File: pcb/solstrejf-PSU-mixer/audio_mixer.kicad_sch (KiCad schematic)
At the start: 9 parts, among them U1 Opamp_Dual

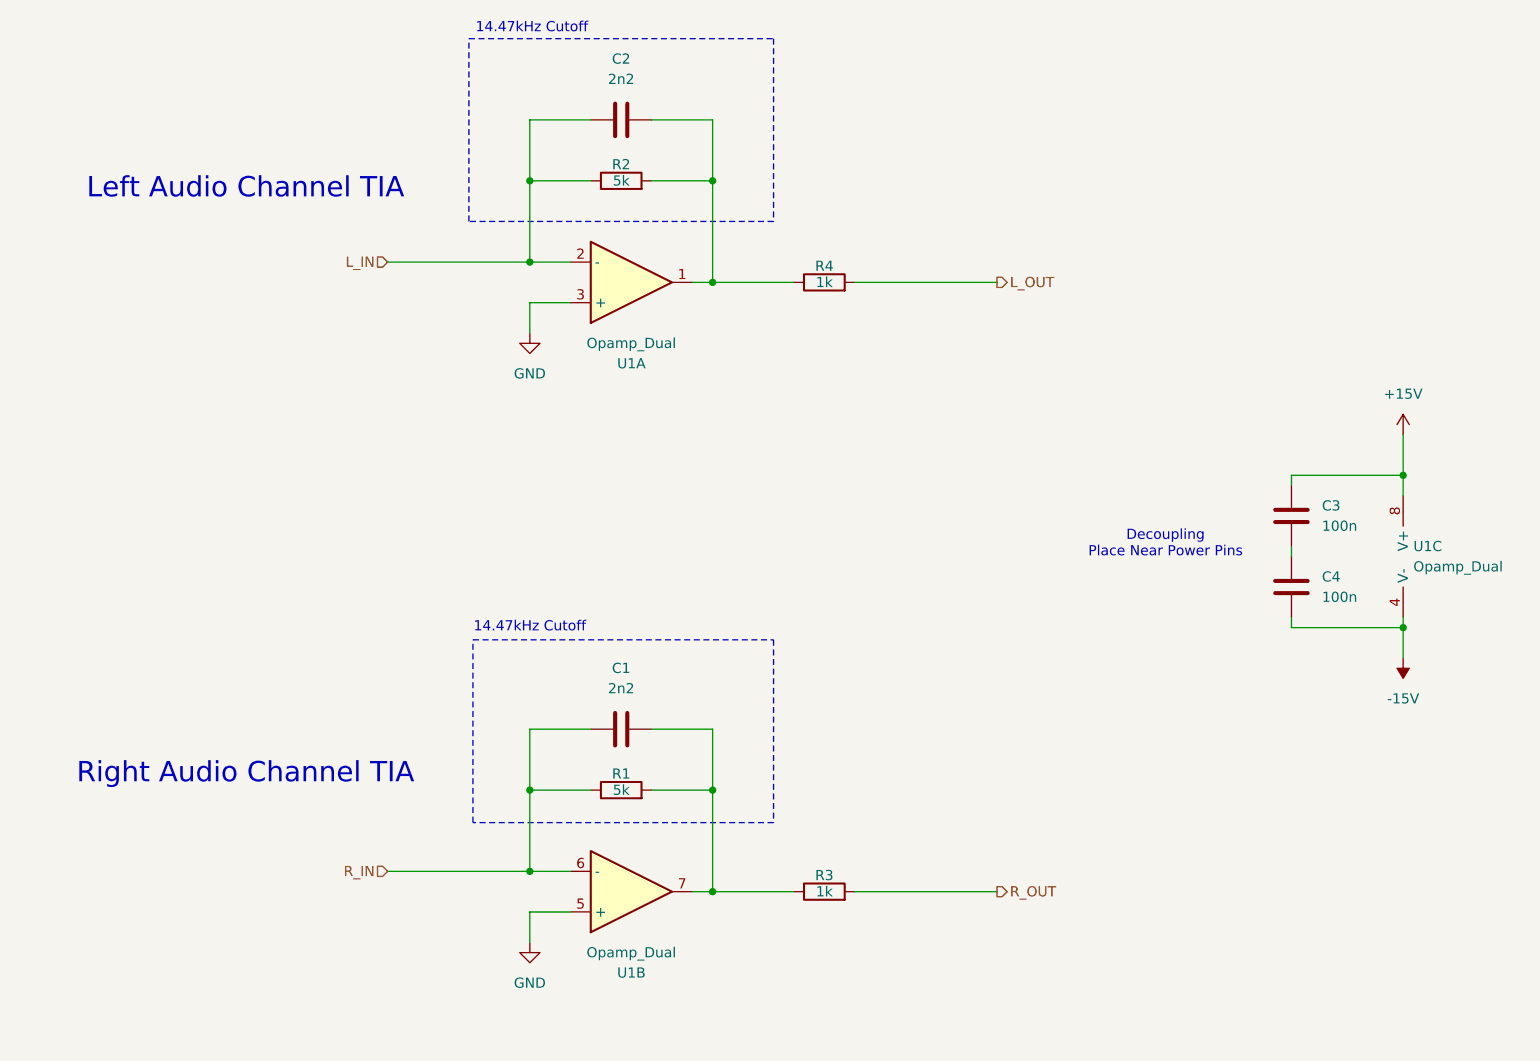
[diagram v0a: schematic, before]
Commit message: updated KiCad schematic and PCB with the new changes added to the TIA after LTspice simulations.
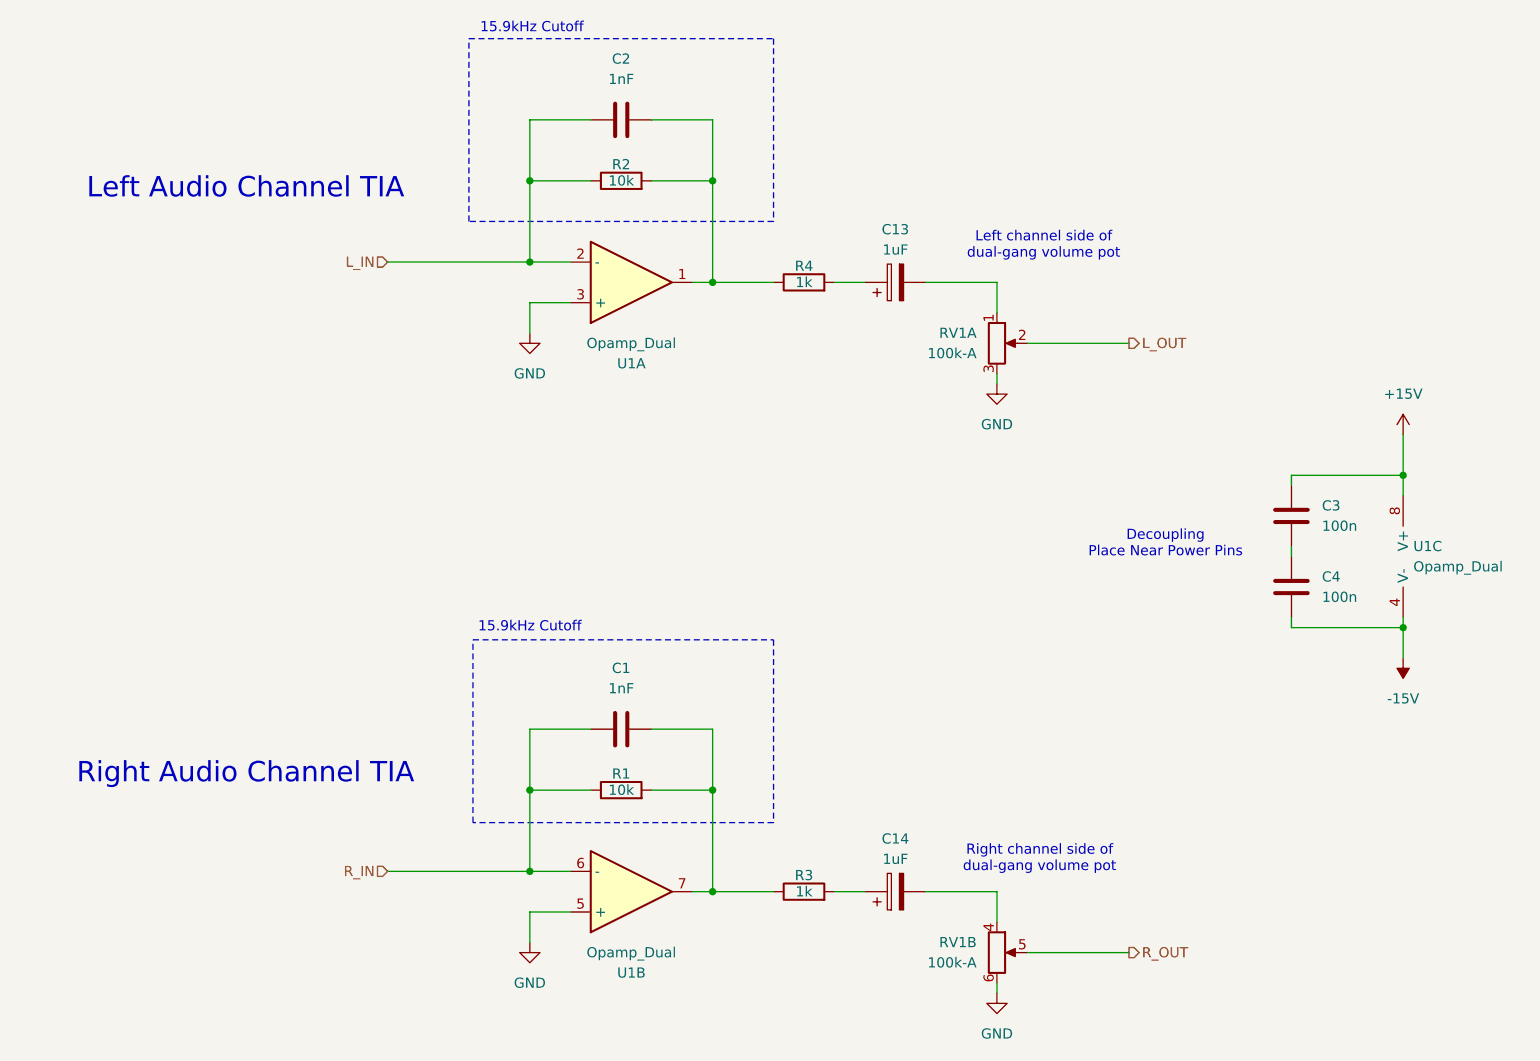
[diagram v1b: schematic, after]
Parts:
- added C13, C14: 1uF, Capacitor_THT:CP_Radial_D5.0mm_P2.00mm, symbol Device:C_Polarized
- added RV1: 100k-A, Connector_PinHeader_2.54mm:PinHeader_2x03_P2.54mm_Vertical, symbol Device:R_Potentiometer_Dual_Separate
- C1, C2: value 2n2 -> 1nF
- R1, R2: value 5k -> 10k
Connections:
- net GND: now also RV1.3, RV1.6
- net L_OUT: now also RV1.2; no longer R4.2
- net R_OUT: now also RV1.5; no longer R3.2
- new net: C14.1, R3.2
- new net: C13.2, RV1.1
- new net: C13.1, R4.2
- new net: C14.2, RV1.4
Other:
- note added: "15.9kHz Cutoff"
- note added: "Left channel side of dual-gang volume pot"
- note added: "Right channel side of dual-gang volume pot"
- note removed: "14.47kHz Cutoff"
- moved on the sheet: R3, R4

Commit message: made first attempt of a PCB layout onf the PSU/mixer. No routing performed. Minor updates to schematic, including mounting holes.
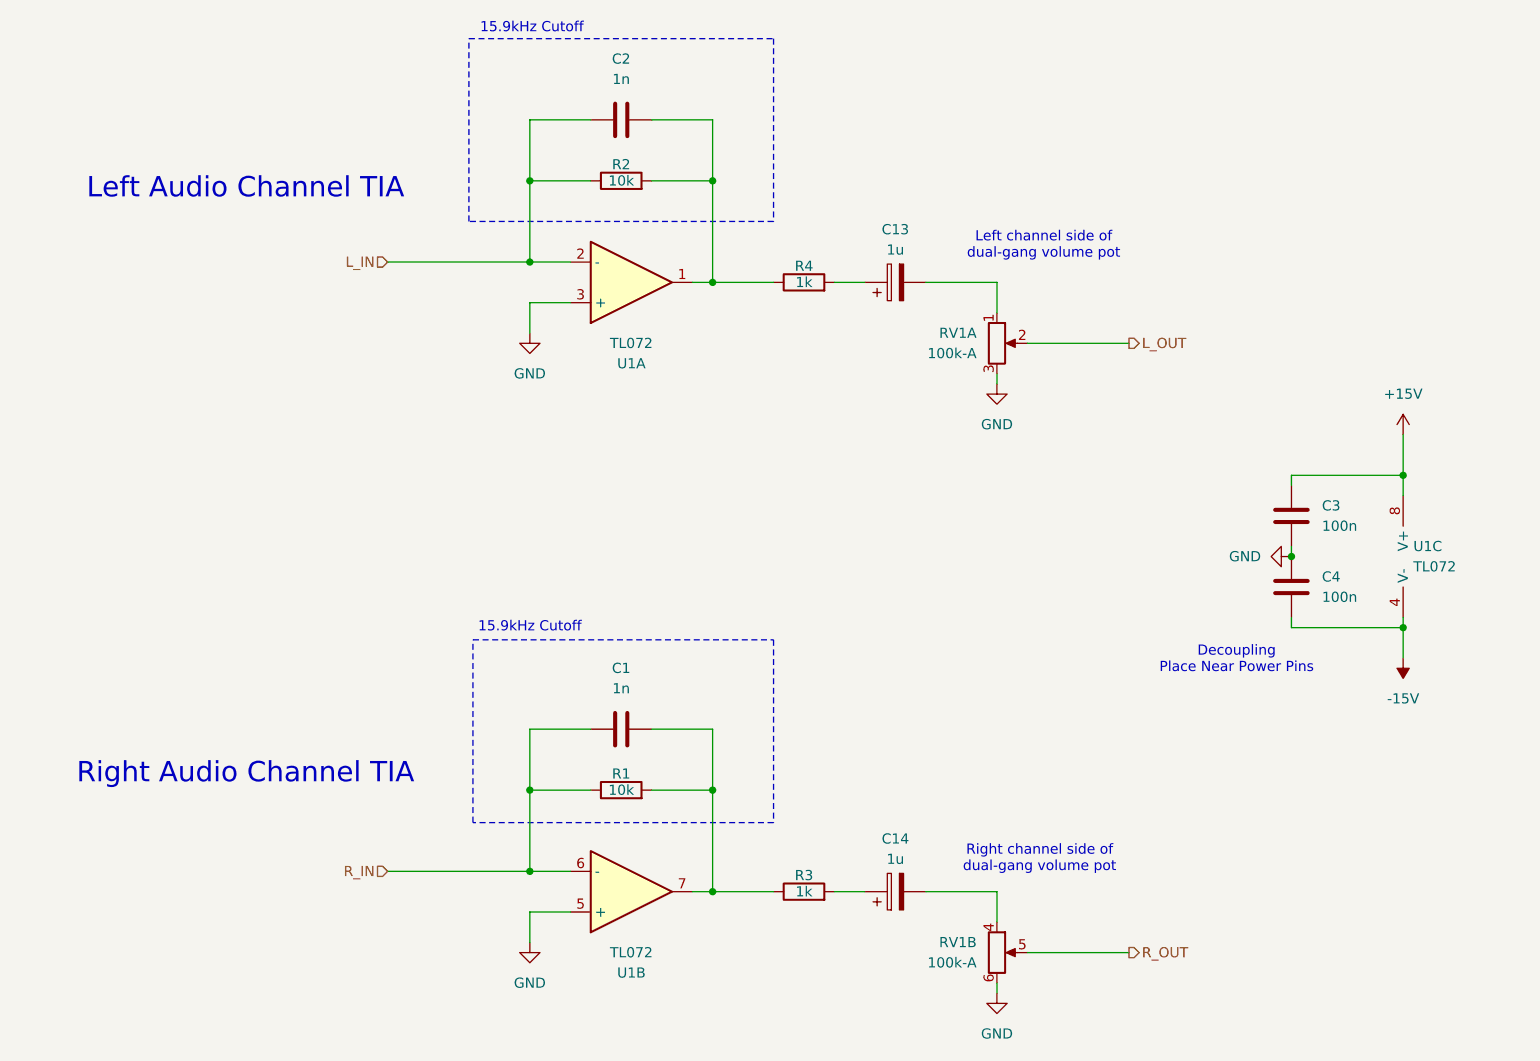
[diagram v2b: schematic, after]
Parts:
- C1, C2: value 1nF -> 1n
- C13, C14: value 1uF -> 1u
- U1: value Opamp_Dual -> TL072
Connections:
- net GND: now also C3.1, C4.2
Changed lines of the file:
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@@
+	)
+	(junction
+		(at 214.63 90.17)
+		(diameter 0)
+		(color 0 0 0 0)
 	)
 	(junction
@@
 	(text "Decoupling\nPlace Near Power Pins"
 		(exclude_from_sim no)
-		(at 198.882 88.646 0)
+		(at 207.772 103.124 0)
 		(effects
 			(font
@@
 	(symbol
 		(lib_id "power:GND")
+		(at 214.63 90.17 270)
+		(unit 1)
+		(exclude_from_sim no)
+		(in_bom yes)
+		(on_board yes)
+		(dnp no)
+		(fields_autoplaced yes)
+		(property "Reference" "#PWR026"
+			(at 208.28 90.17 0)
+			(effects
+				(font
+					(size 1.27 1.27)
+				)
+				(hide yes)
+			)
+		)
+		(property "Value" "GND"
+			(at 210.82 90.1699 90)
+			(effects
+				(font
+					(size 1.27 1.27)
+				)
+				(justify right)
+			)
+		)
+		(property "Footprint" ""
+			(at 214.63 90.17 0)
+			(effects
+				(font
+					(size 1.27 1.27)
+				)
+				(hide yes)
+			)
+		)
+		(property "Datasheet" ""
+			(at 214.63 90.17 0)
+			(effects
+				(font
+					(size 1.27 1.27)
+				)
+				(hide yes)
+			)
+		)
+		(property "Description" "Power symbol creates a global label with name \"GND\" , ground"
+			(at 214.63 90.17 0)
+			(effects
+				(font
+					(size 1.27 1.27)
+				)
+				(hide yes)
+			)
+		)
+		(pin "1"
+		)
+		(instances
+			(project "solstrejf-PSU-mixer"
+				(path "/af6d8e61-e5bb-4f8a-a3f3-03014b8b6dd9/0a99becb-17cc-44aa-8430-edab444b5bb9"
+					(reference "#PWR026")
+					(unit 1)
+				)
+			)
+		)
+	)
+	(symbol
+		(lib_id "power:GND")
 		(at 177.8 68.58 0)
 		(unit 1)
@@
 			)
 		)
-		(property "Value" "Opamp_Dual"
+		(property "Value" "TL072"
 			(at 132.08 63.5 0)
 			(effects
@@
 			)
 		)
-		(property "Value" "Opamp_Dual"
+		(property "Value" "TL072"
 			(at 132.08 139.7 0)
 			(effects
@@
 			)
 		)
-		(property "Value" "1uF"
+		(property "Value" "1u"
 			(at 165.1 51.816 90)
 			(effects
@@
 			)
 		)
-		(property "Value" "Opamp_Dual"
+		(property "Value" "TL072"
 			(at 229.87 91.4399 0)
 			(effects
@@
 			)
 		)
-		(property "Value" "1uF"
+		(property "Value" "1u"
 			(at 165.1 128.016 90)
 			(effects
@@
 			)
 		)
-		(property "Value" "1nF"
+		(property "Value" "1n"
 			(at 130.81 106.68 90)
 			(effects
@@
 			)
 		)
-		(property "Value" "1nF"
+		(property "Value" "1n"
 			(at 130.81 30.48 90)
 			(effects

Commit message: Updated fonts in PSU+mixer schematic. Added a print of the PSU+mixer schemtic in new  directory.
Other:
- title: (none) -> Left & Right Channel Audio Mixer
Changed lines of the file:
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@@
 	(generator_version "8.0")
 	(paper "A4")
+	(title_block
+		(title "Left & Right Channel Audio Mixer")
+		(date "2024-08-24")
+		(rev "1.0")
+	)
 	(junction
 		(at 142.24 43.18)

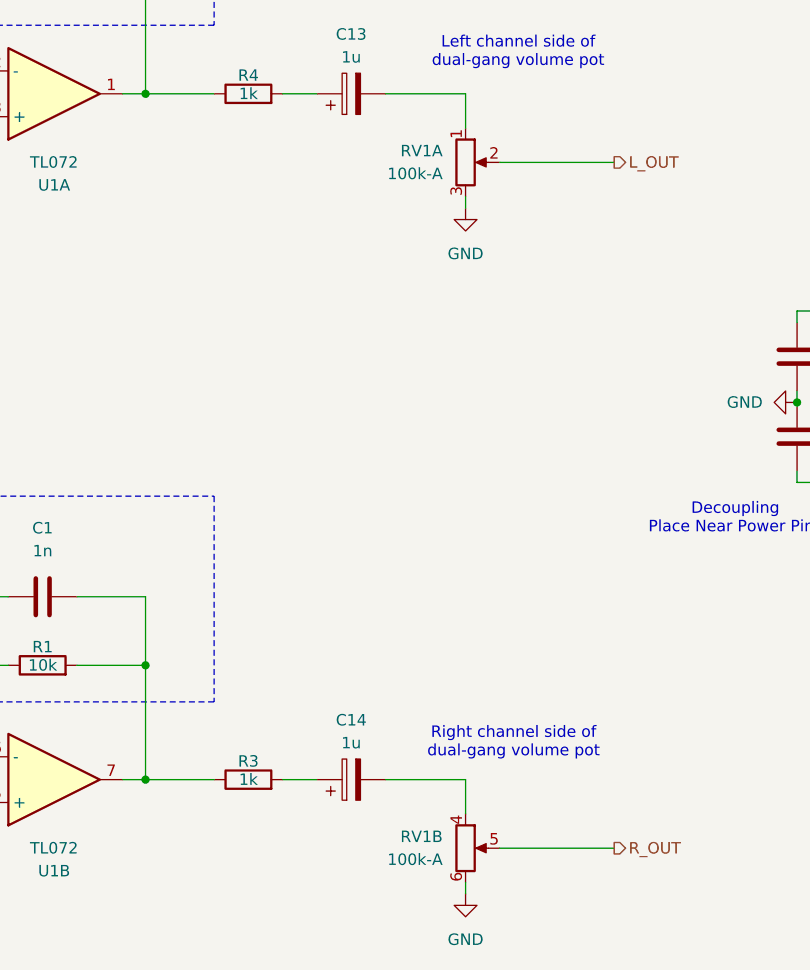
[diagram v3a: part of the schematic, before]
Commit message: Updated LTspice simulation of output TIA with decrease volume pot for 15.92Hz highpass frequency. Updated KiCad and images with the same change.
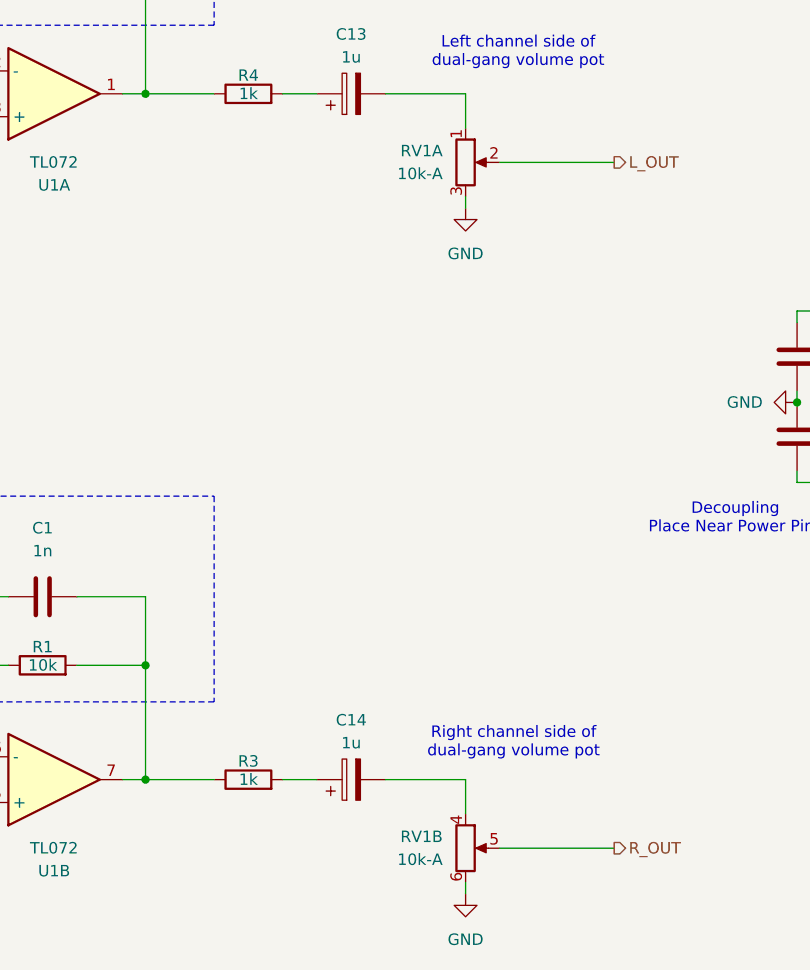
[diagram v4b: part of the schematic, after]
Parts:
- RV1: value 100k-A -> 10k-A
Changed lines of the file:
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@@
 			)
 		)
-		(property "Value" "100k-A"
+		(property "Value" "10k-A"
 			(at 175.26 64.7699 0)
 			(effects
@@
 			)
 		)
-		(property "Value" "100k-A"
+		(property "Value" "10k-A"
 			(at 175.26 140.9699 0)
 			(effects
